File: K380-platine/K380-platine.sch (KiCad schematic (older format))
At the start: 6 parts, among them J1 JST-PH 2, J2 Conn_01x23, J3 MicroMod-M.2E, Q1 PMost Enc FET -20V, U1 XC6220B331MR, U2 MCP73831-2-OT

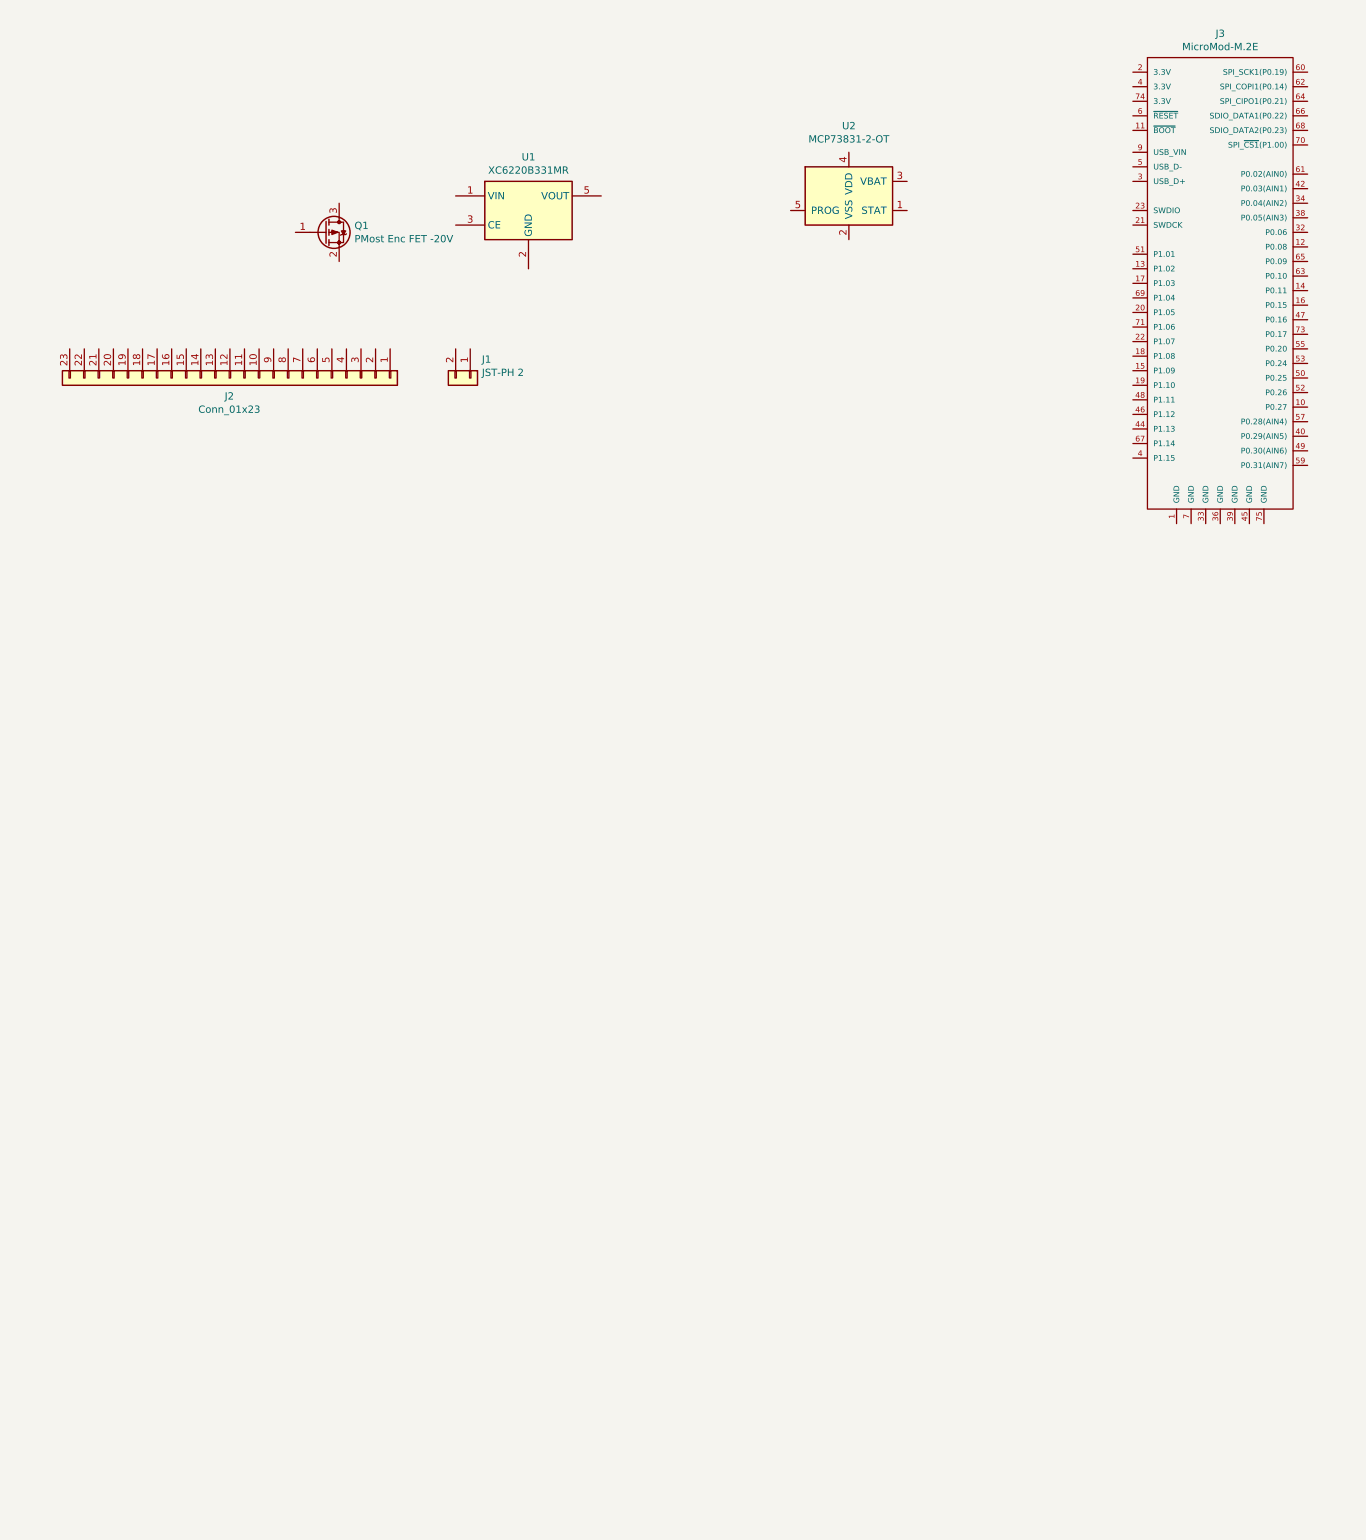
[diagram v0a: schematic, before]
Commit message: Schem: Add Power and Charging Circuit
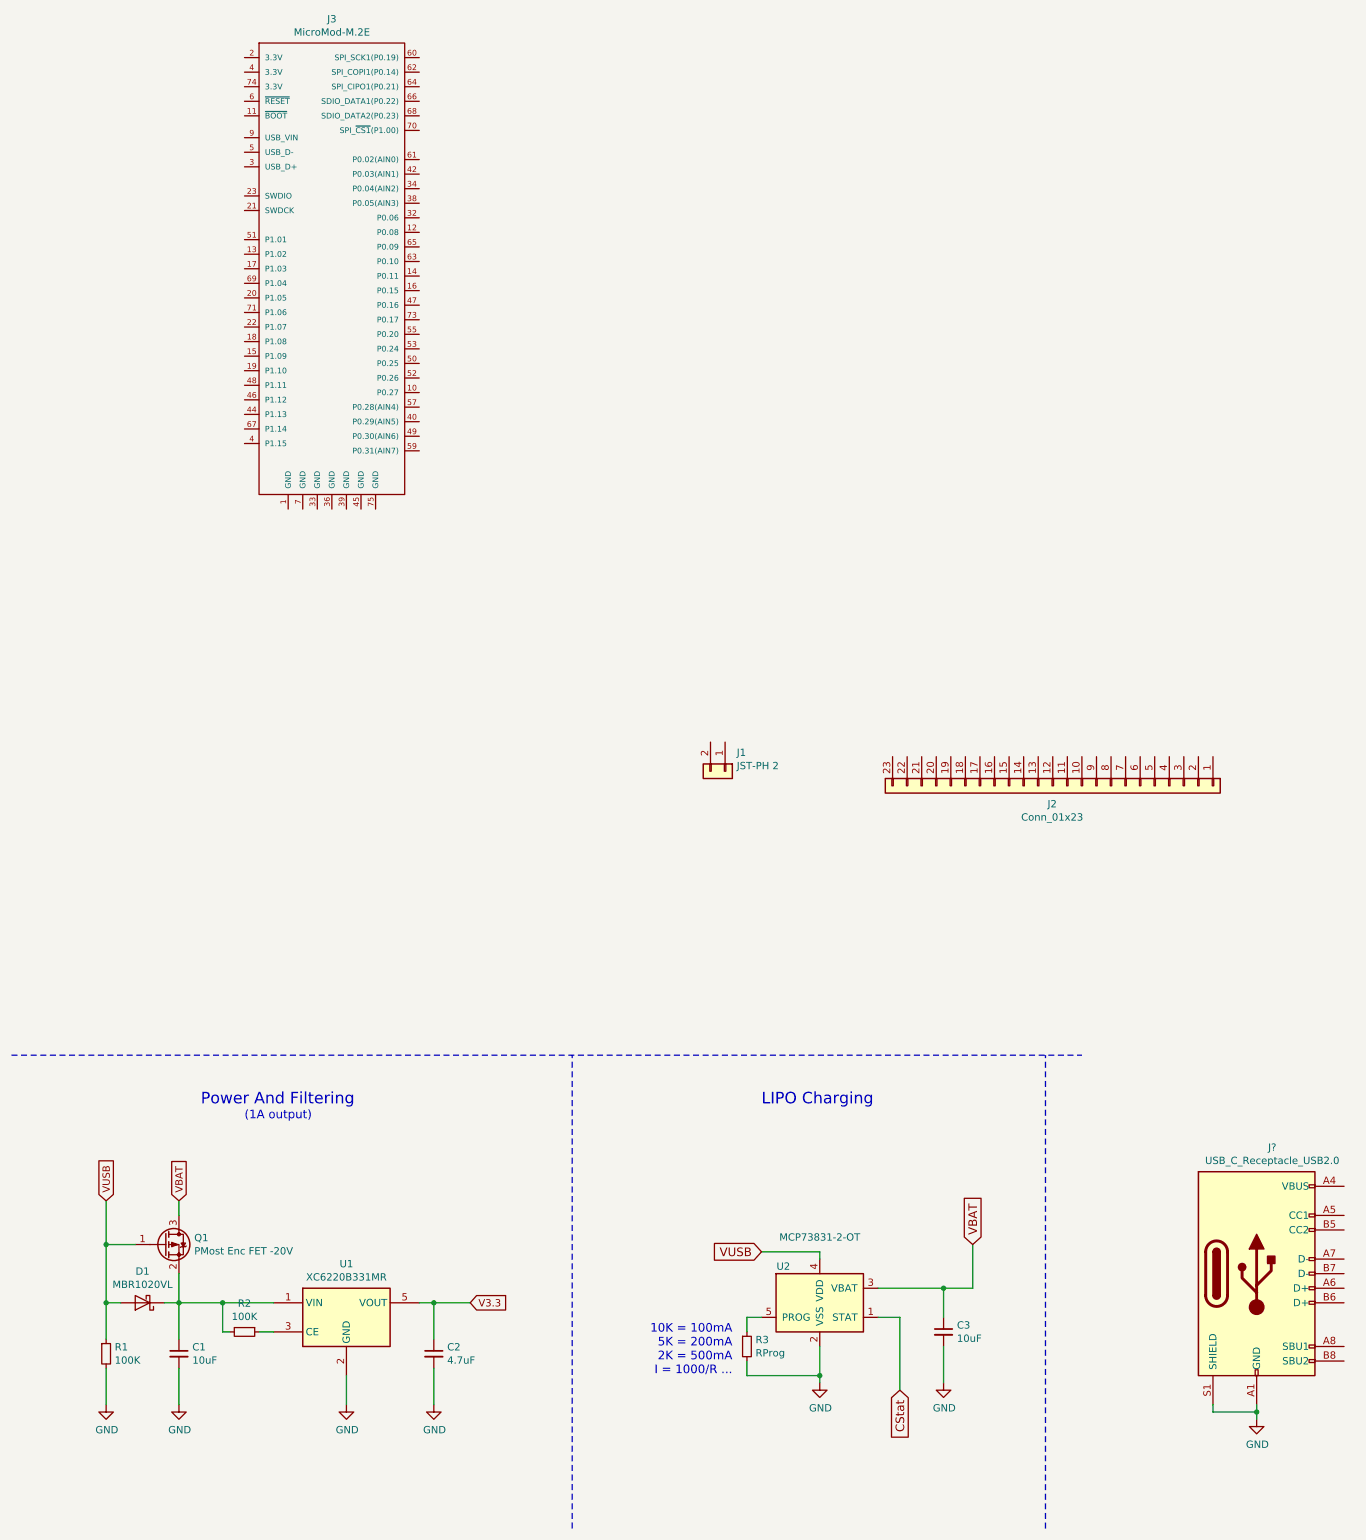
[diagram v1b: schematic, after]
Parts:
- added C1, C3: 10uF, symbol Device:C_Small
- added C2: 4.7uF, symbol Device:C_Small
- added D1: MBR1020VL, Diode_SMD:D_SOD-123F, symbol Diode:MBR1020VL
- added J?: USB_C_Receptacle_USB2.0, symbol Connector:USB_C_Receptacle_USB2.0
- added R1, R2: 100K, symbol Device:R_Small
- added R3: RProg, symbol Device:R_Small
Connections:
- net VUSB: now reaches Q1.1 (G)
- net VUSB: now also U2.4 (VDD), D1.2 (A), R1.1
- net at Q1.2 (S): now also U1.1 (VIN), C1.1, D1.1 (K), R2.2
- net VBAT: now reaches Q1.3 (D)
- net VBAT: now also U2.3 (VBAT), C3.1
- net GND: now reaches U1.2 (GND)
- net GND: now also U2.2 (VSS), C1.2, C2.2, C3.2, J?.A1 (GND), J?.A12 (GND), J?.B1 (GND), J?.B12 (GND), J?.S1 (SHIELD), R1.2, R3.2
- net at U1.3 (CE): now also R2.1
- net V3.3: now reaches U1.5 (VOUT)
- net V3.3: now also C2.1
- net CStat: now reaches U2.1 (STAT)
- net at U2.5 (PROG): now also R3.1
- new net: J?.A4 (VBUS), J?.A9 (VBUS), J?.B4 (VBUS), J?.B9 (VBUS)
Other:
- note added: "(1A output)"
- note added: "10K = 100mA\n5K = 200mA\n2K = 500mA\nI = 1000/R ..."
- note added: "LIPO Charging"
- note added: "Power And Filtering"
- moved on the sheet: J1, J2, J3, Q1, U1, U2

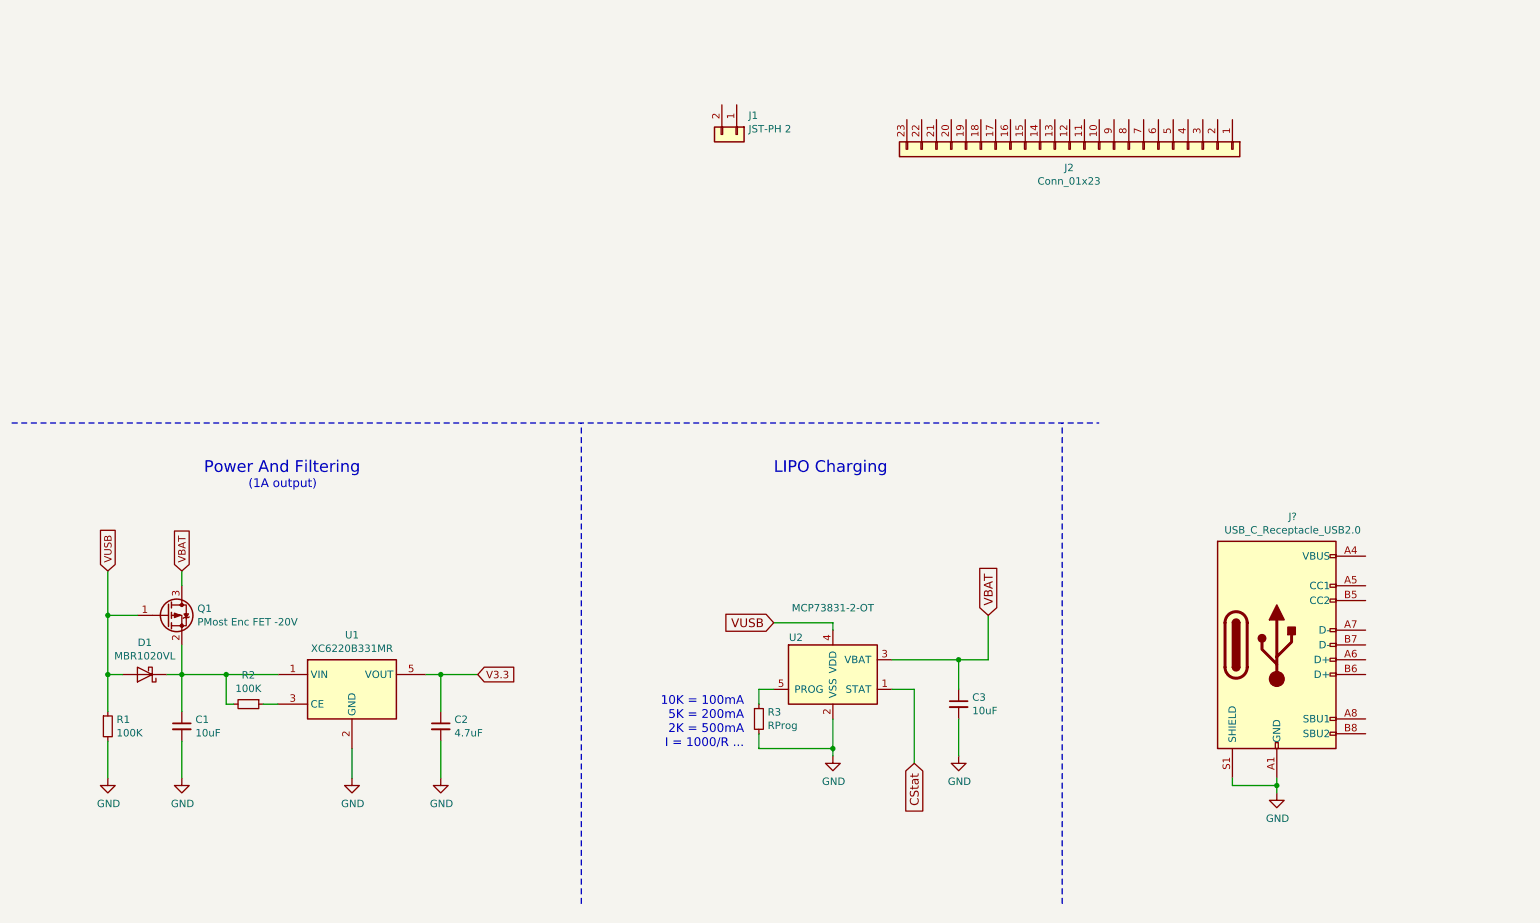
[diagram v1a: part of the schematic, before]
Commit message: Wired USB-C
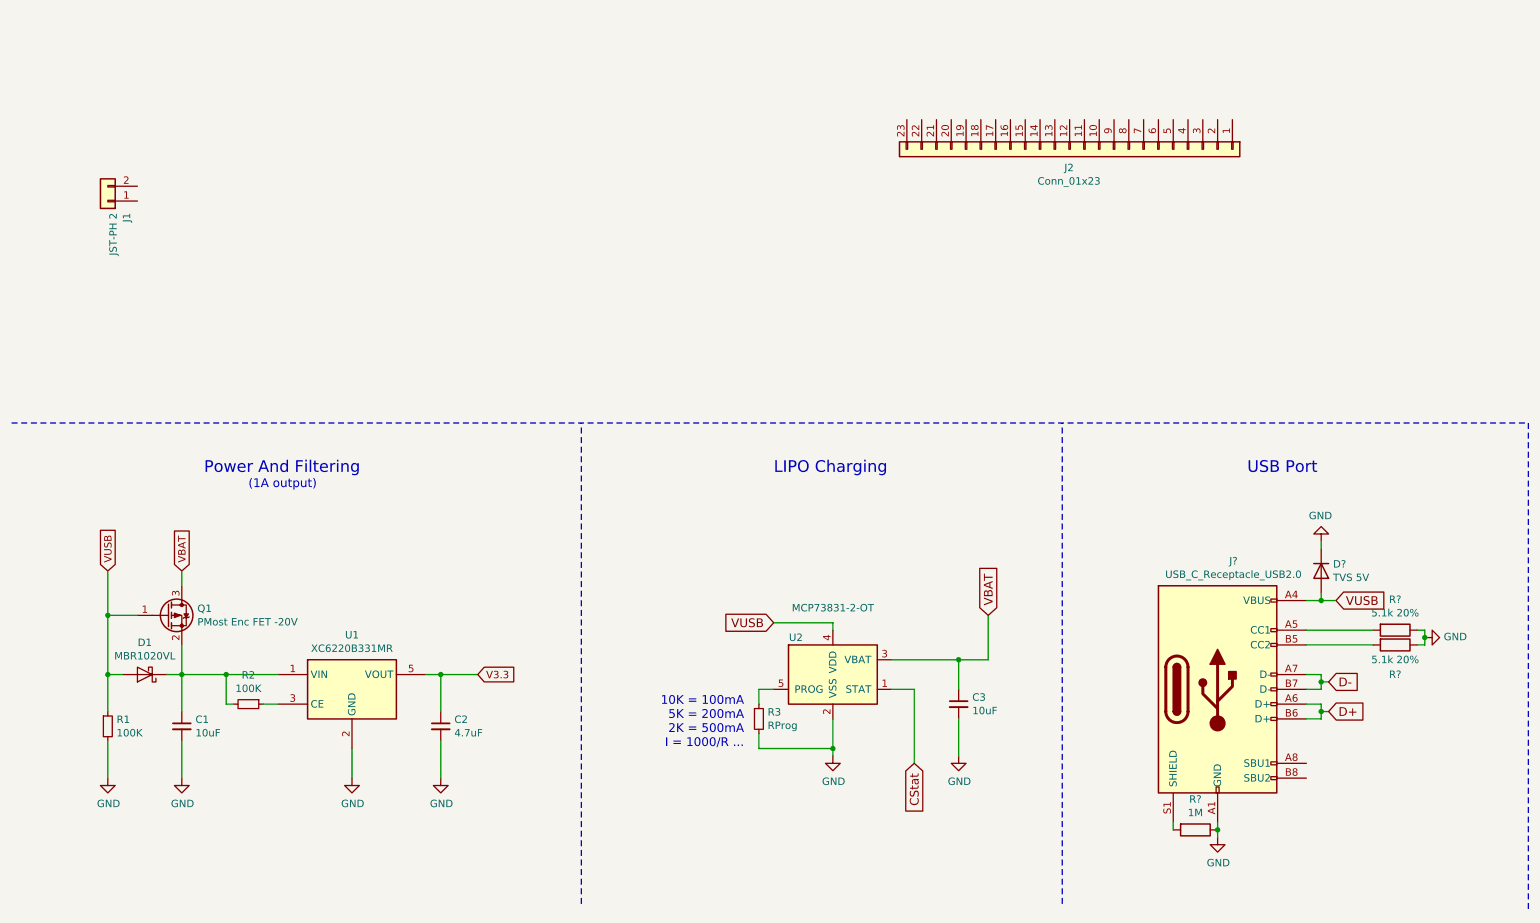
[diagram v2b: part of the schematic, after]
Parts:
- added D?: TVS 5V, symbol Device:D
- added R?: 1M, symbol Device:R
- added R? (x2): 5.1k 20%, symbol Device:R
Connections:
- net GND: now also D?.1 (K), R?.1, R?.1, R?.1; no longer J?.S1 (SHIELD)
- net VUSB: now also J?.A4 (VBUS), J?.A9 (VBUS), J?.B4 (VBUS), J?.B9 (VBUS), D?.2 (A)
- net at J?.A5 (CC1): now also R?.2
- net D+: now reaches J?.A6 (D+)
- net D+: now also J?.B6 (D+)
- net D-: now reaches J?.A7 (D-)
- net D-: now also J?.B7 (D-)
- net at J?.B5 (CC2): now also R?.2
- new net: J?.S1 (SHIELD), R?.2
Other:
- note added: "USB Port"
- moved on the sheet: J1, J?
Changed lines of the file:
@@
-$EndComp
-$Comp
-L Connector_Generic:Conn_01x02 J1
-U 1 1 62903AF0
-P 5400 6000
-F 0 "J1" V 5272 6080 50  0000 L CNN
-F 1 "JST-PH 2" V 5363 6080 50  0000 L CNN
-F 2 "Connector_JST:JST_PH_S2B-PH-SM4-TB_1x02-1MP_P2.00mm_Horizontal" H 5400 6000 50  0001 C CNN
-F 3 "~" H 5400 6000 50  0001 C CNN
-	1    5400 6000
-	0    1    1    0
 $EndComp
 $Comp
@@
 Text Notes 5650 8300 0    79   ~ 0
 LIPO Charging
-Wire Notes Line
-	500  7950 7850 7950
 Wire Wire Line
 	6450 9750 6600 9750
@@
 L power:GND #PWR?
 U 1 1 62947FF0
-P 9050 10450
-F 0 "#PWR?" H 9050 10200 50  0001 C CNN
-F 1 "GND" H 9055 10277 50  0000 C CNN
-F 2 "" H 9050 10450 50  0001 C CNN
-F 3 "" H 9050 10450 50  0001 C CNN
-	1    9050 10450
-	1    0    0    -1
-$EndComp
-Wire Wire Line
-	9050 10450 9050 10400
-Wire Wire Line
-	8750 10350 8750 10400
-Wire Wire Line
-	8750 10400 9050 10400
-Connection ~ 9050 10400
-Wire Wire Line
-	9050 10400 9050 10350
+P 8650 10750
+F 0 "#PWR?" H 8650 10500 50  0001 C CNN
+F 1 "GND" H 8655 10577 50  0000 C CNN
+F 2 "" H 8650 10750 50  0001 C CNN
+F 3 "" H 8650 10750 50  0001 C CNN
+	1    8650 10750
+	1    0    0    -1
+$EndComp
 $Comp
 L Connector:USB_C_Receptacle_USB2.0 J?
 U 1 1 62949AC6
-P 9050 9450
-F 0 "J?" H 9157 10317 50  0000 C CNN
-F 1 "USB_C_Receptacle_USB2.0" H 9157 10226 50  0000 C CNN
-F 2 "" H 9200 9450 50  0001 C CNN
-F 3 "https://www.usb.org/sites/default/files/documents/usb_type-c.zip" H 9200 9450 50  0001 C CNN
-	1    9050 9450
-	1    0    0    -1
+P 8650 9750
+F 0 "J?" H 8757 10617 50  0000 C CNN
+F 1 "USB_C_Receptacle_USB2.0" H 8757 10526 50  0000 C CNN
+F 2 "" H 8800 9750 50  0001 C CNN
+F 3 "https://www.usb.org/sites/default/files/documents/usb_type-c.zip" H 8800 9750 50  0001 C CNN
+	1    8650 9750
+	1    0    0    -1
+$EndComp
+Text GLabel 9450 9150 2    59   Input ~ 0
+VUSB
+$Comp
+L power:GND #PWR?
+U 1 1 6295443F
+P 9350 8750
+F 0 "#PWR?" H 9350 8500 50  0001 C CNN
+F 1 "GND" H 9355 8577 50  0000 C CNN
+F 2 "" H 9350 8750 50  0001 C CNN
+F 3 "" H 9350 8750 50  0001 C CNN
+	1    9350 8750
+	-1   0    0    1
+$EndComp
+$Comp
+L Device:D D?
+U 1 1 62955F4D
+P 9350 8950
+F 0 "D?" V 9304 9030 50  0000 L CNN
+F 1 "TVS 5V" V 9395 9030 50  0000 L CNN
+F 2 "" H 9350 8950 50  0001 C CNN
+F 3 "~" H 9350 8950 50  0001 C CNN
+	1    9350 8950
+	0    1    1    0
+$EndComp
+Wire Wire Line
+	8650 10650 8650 10700
+$Comp
+L Device:R R?
+U 1 1 62957FD7
+P 8500 10700
+F 0 "R?" V 8293 10700 50  0000 C CNN
+F 1 "1M" V 8384 10700 50  0000 C CNN
+F 2 "" V 8430 10700 50  0001 C CNN
+F 3 "~" H 8500 10700 50  0001 C CNN
+	1    8500 10700
+	0    1    1    0
+$EndComp
+Connection ~ 8650 10700
+Wire Wire Line
+	8650 10700 8650 10750
+Wire Wire Line
+	8350 10700 8350 10650
+$Comp
+L Device:R R?
+U 1 1 62959392
+P 9850 9350
+F 0 "R?" V 9643 9350 50  0000 C CNN
+F 1 "5.1k 20%" V 9734 9350 50  0000 C CNN
+F 2 "" V 9780 9350 50  0001 C CNN
+F 3 "~" H 9850 9350 50  0001 C CNN
+	1    9850 9350
+	0    1    1    0
+$EndComp
+$Comp
+L Device:R R?
+U 1 1 62959A27
+P 9850 9450
+F 0 "R?" V 10050 9450 50  0000 C CNN
+F 1 "5.1k 20%" V 9950 9450 50  0000 C CNN
+F 2 "" V 9780 9450 50  0001 C CNN
+F 3 "~" H 9850 9450 50  0001 C CNN
+	1    9850 9450
+	0    1    1    0
+$EndComp
+$Comp
+L power:GND #PWR?
+U 1 1 6295B4CE
+P 10050 9400
+F 0 "#PWR?" H 10050 9150 50  0001 C CNN
+F 1 "GND" V 10055 9272 50  0000 R CNN
+F 2 "" H 10050 9400 50  0001 C CNN
+F 3 "" H 10050 9400 50  0001 C CNN
+	1    10050 9400
+	0    -1   -1   0
+$EndComp
+Wire Wire Line
+	10000 9350 10050 9350
+Wire Wire Line
+	10050 9450 10000 9450
+Wire Wire Line
+	9250 9350 9700 9350
+Wire Wire Line
+	9250 9450 9700 9450
+Wire Wire Line
+	9350 8800 9350 8750
+Wire Wire Line
+	9250 9150 9350 9150
+Wire Wire Line
+	9350 9150 9350 9100
+Connection ~ 9350 9150
+Wire Wire Line
+	9350 9150 9450 9150
+Wire Wire Line
+	10050 9350 10050 9400
+Connection ~ 10050 9400
+Wire Wire Line
+	10050 9400 10050 9450
+Text GLabel 9400 9700 2    59   Input ~ 0
+D-
+Text GLabel 9400 9900 2    59   Input ~ 0
+D+
+Wire Wire Line
+	9250 9950 9350 9950
+Wire Wire Line
+	9250 9850 9350 9850
+Wire Wire Line
+	9250 9750 9350 9750
+Wire Wire Line
+	9250 9650 9350 9650
+Wire Wire Line
+	9350 9650 9350 9700
+Wire Wire Line
+	9350 9850 9350 9900
+Wire Wire Line
+	9350 9700 9400 9700
+Connection ~ 9350 9700
+Wire Wire Line
+	9350 9700 9350 9750
+Wire Wire Line
+	9350 9900 9400 9900
+Connection ~ 9350 9900
+Wire Wire Line
+	9350 9900 9350 9950
+Text Notes 8850 8300 0    79   ~ 0
+USB Port
+Wire Notes Line
+	10750 7950 10750 11250
+Wire Notes Line
+	500  7950 10750 7950
+$Comp
+L Connector_Generic:Conn_01x02 J1
+U 1 1 62903AF0
+P 1150 6450
+F 0 "J1" V 1022 6530 50  0000 L CNN
+F 1 "JST-PH 2" V 1113 6530 50  0000 L CNN
+F 2 "Connector_JST:JST_PH_S2B-PH-SM4-TB_1x02-1MP_P2.00mm_Horizontal" H 1150 6450 50  0001 C CNN
+F 3 "~" H 1150 6450 50  0001 C CNN
+	1    1150 6450
+	-1   0    0    1
 $EndComp
 $EndSCHEMATC

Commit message: Add battery con and user switches
- changed schematic page design
- battery can be disabled via slider switch
  - integrated library loader
- add user and reset switch
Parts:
- added Q2: Q_NMOS_DGS, symbol Device:Q_NMOS_DGS
- added R7: 100K, symbol Device:R
- added R? (x2): 100K, symbol Device:R_Small
- added SW?: EG1215AA, LibraryLoader:EG1215AA, symbol Switch:SW_DPST_x2
- added SW? (x2): SW_Push, symbol Switch:SW_Push
- gave numbers to parts that had none: 5
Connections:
- net GND: now also J1.1 (Pin_1), R?.2, SW?.1, SW?.1
- net VBAT: now also J1.2 (Pin_2), Q2.3 (S), R?.1, SW?.1 (A); no longer Q1.3 (D)
- new net: Q1.3 (D), Q2.1 (D)
- new net: Q2.2 (G), R7.1
- new net: R7.2, SW?.2 (B)
- new net RESET: SW?.2
- new net SWITCH: SW?.2
- new net VDIV: R?.1, R?.2
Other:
- note added: "JST PH LiPo Input"
- note added: "Reset/User Switch"
- moved on the sheet: C1, C2, D1, J1, Q1, R1, R2, U1
